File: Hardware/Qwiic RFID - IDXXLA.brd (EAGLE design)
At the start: 25.4 x 34.3 mm, 51 parts, among them J2 SMD, J3 PTH, J4 SMD, J8 AVR_SPI_PROG_3X2TESTPOINTS, Q1 600mA/40V, U1 ATTINY84, U2 ID-12/20SMD

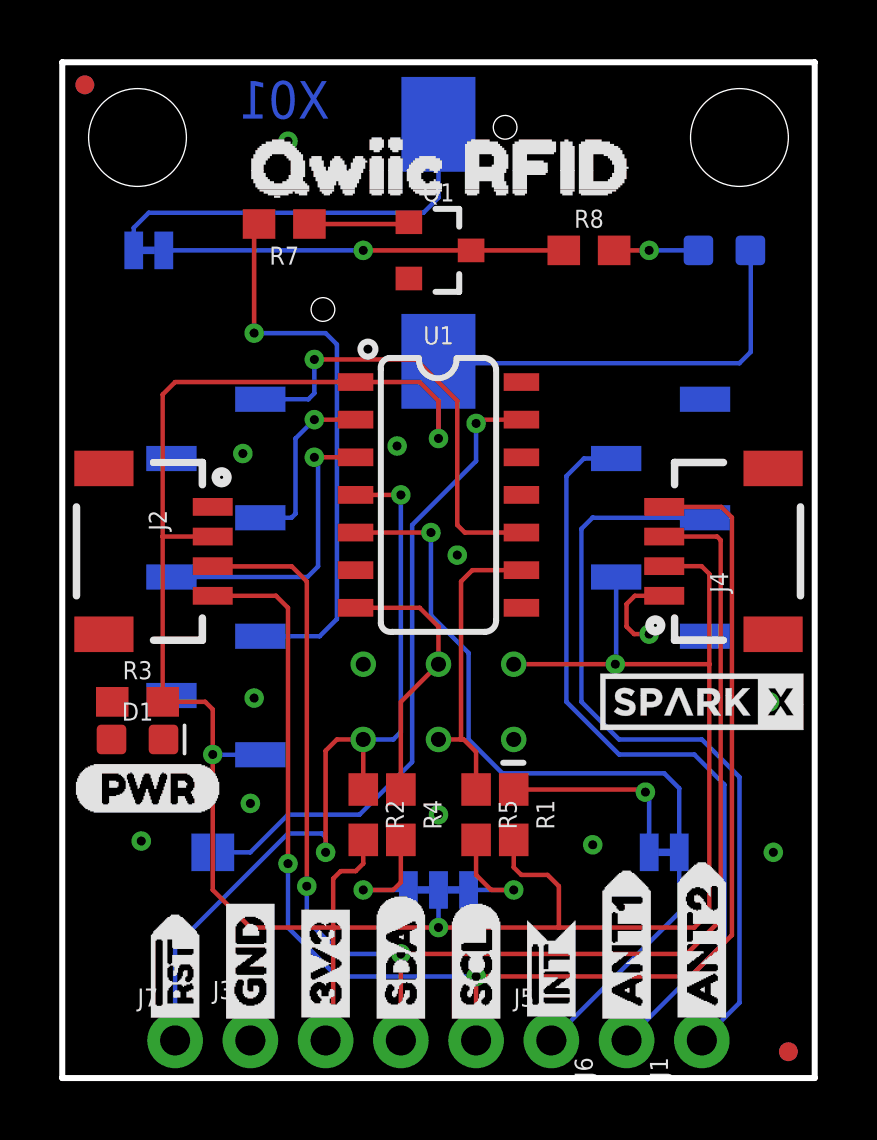
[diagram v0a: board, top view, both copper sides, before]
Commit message: More compact
Shrunk 10 mil, beefed up 3.3V lines to 10 mil
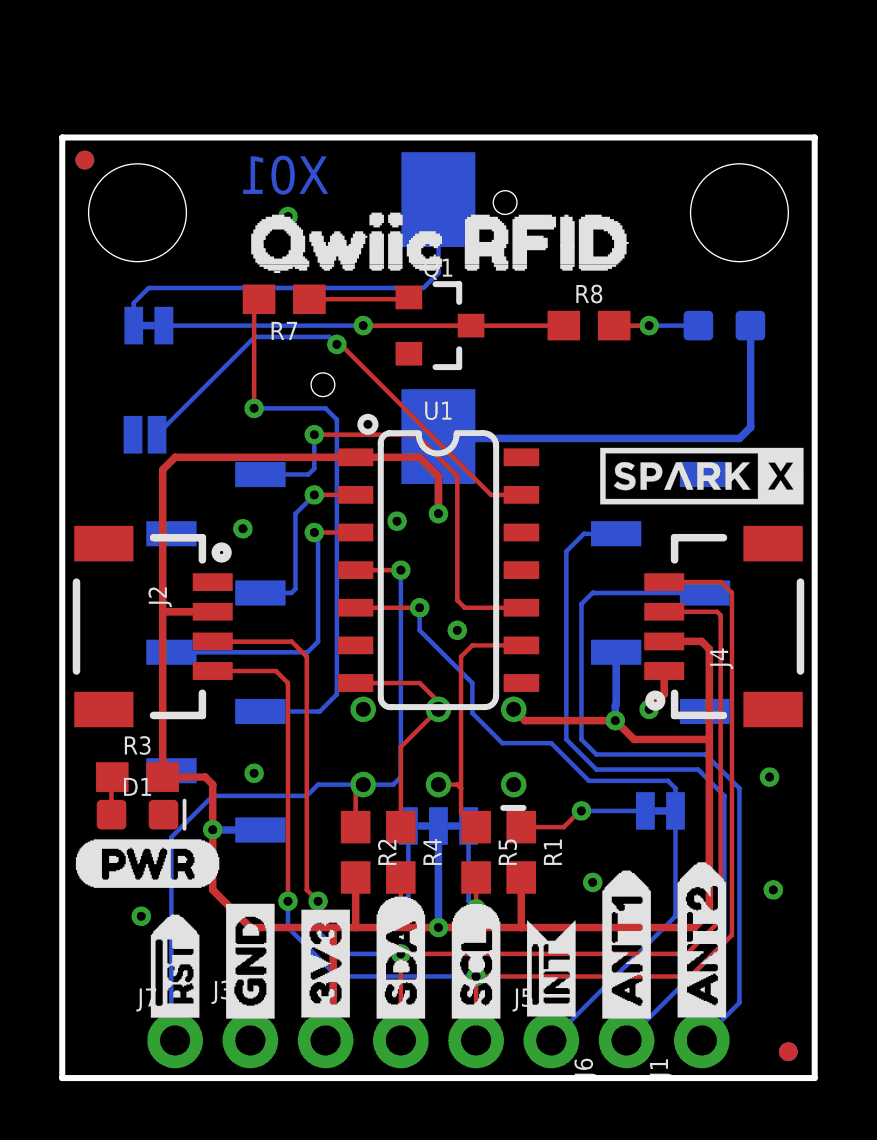
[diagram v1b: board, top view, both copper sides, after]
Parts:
- removed U$14: (no value), Labels:ADR-()
- added U$20: (no value), ANT1:ANT10
- added U$21: (no value), Labels:INT#-[<
- added U$22: (no value), Labels:SCL-[)
- added U$23: (no value), Labels:SDA-[)
- added U$24: (no value), Labels:3V3-04
- added U$25: (no value), Labels:GND-04
- added U$26: (no value), Labels:RST#-[>
- added U$3: (no value), ANT2:ANT20
- U$12: device Labels:I2C-() -> ADR3:ADR0
- U$13: device Labels:INT-() -> INT3:INT0
- U$2: device SparkX:SPARKX-SMALL -> Labels:I_SUPER2_C-()-03
- moved LOGO1 20.3 mm to (18.9, 29.8)
- moved U$12 18.7 mm to (4.70, 19.9)
- moved JP7 14.3 mm to (2.79, 21.7)
- moved U$2 7.73 mm to (14.1, 10.8)
- moved U$4 7.62 mm to (21.6, 20.3)
- moved U$13 5.39 mm to (21.7, 10.9)
- moved D2 2.54 mm to (22.4, 25.4)
- moved JP9 2.54 mm to (2.92, 25.4)
- moved Q1 2.54 mm to (12.7, 25.4)
- moved R8 2.54 mm to (17.8, 25.4)
- moved U$18 2.54 mm to (25.1, 23.7)
- moved U$19 2.54 mm to (4.70, 28.2)
- moved J2 2.54 mm to (5.08, 15.2)
- moved J4 2.54 mm to (20.3, 15.2)
- moved U$1 2.54 mm to (0.38, 7.24)
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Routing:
- net 3.3V: track 102.5 -> 94.9 mm
- net N$6: track 21.5 -> 15.9 mm
- net SDA: track 47.9 -> 42.9 mm
- net SCL: track 49.1 -> 44.0 mm
- net !INT: track 28.2 -> 24.7 mm
- net !RST: track 27.8 -> 25.6 mm, vias 2 -> 1
- net N$4: track 6.57 -> 4.42 mm
- net ANT2: track 26.0 -> 24.0 mm
- net ANT1: track 26.0 -> 24.0 mm
- net GND: track 3.01 -> 1.50 mm, vias 12 -> 10
- net N$3: track 0.00 -> 1.28 mm
- net SDA/MOSI: track 9.09 -> 7.82 mm
- net SCL/SCK: track 10.2 -> 8.97 mm
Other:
- board size 25.4 x 34.3 mm -> 25.4 x 31.8 mm

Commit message: 5 mil smaller
Moved power LED around, squished the PCB a little more.
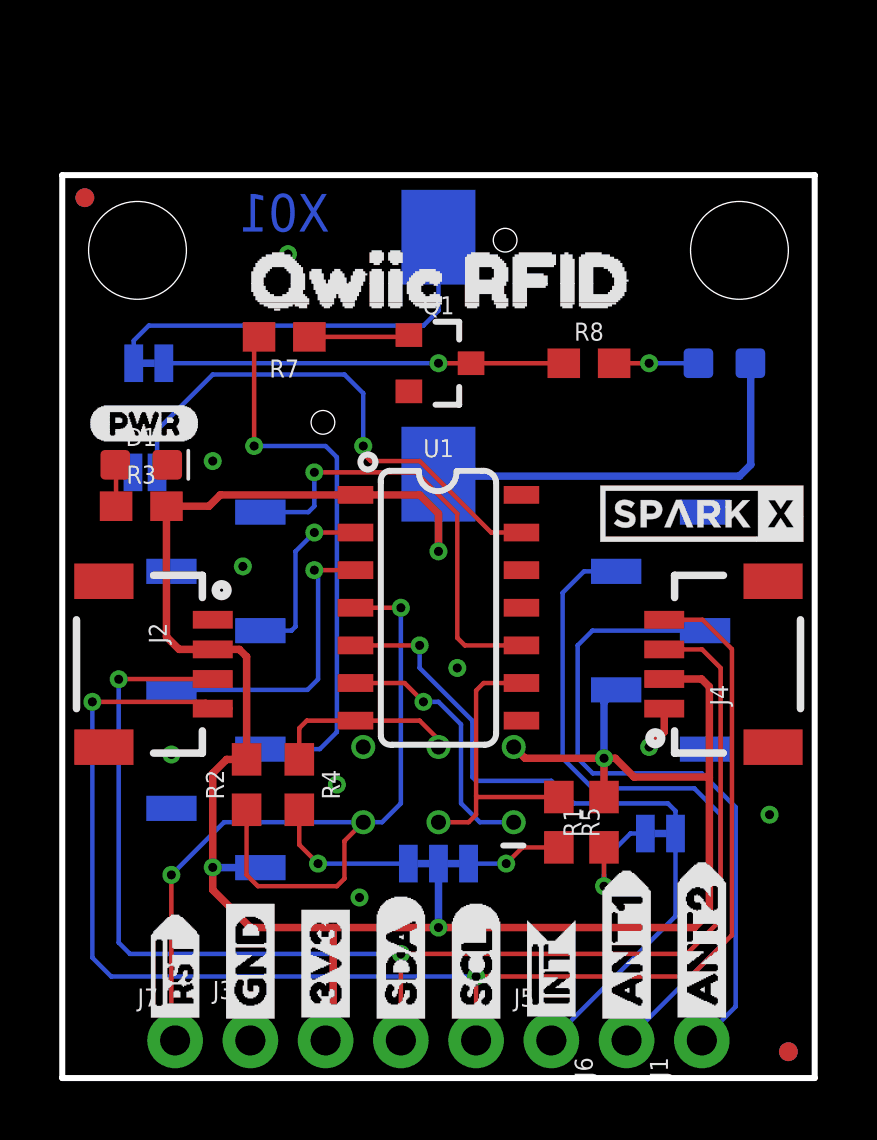
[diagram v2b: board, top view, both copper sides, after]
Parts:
- added U$14: (no value), Labels:PWR-()-03
- U$1: device Labels:PWR-()-04 -> SparkX:SPARKX-TINY
- moved U$1 23.1 mm to (7.62, 29.2), flipped to the bottom
- moved D1 11.8 mm to (2.67, 20.7)
- moved R3 9.14 mm to (2.67, 19.3)
- moved U$13 5.50 mm to (18.2, 6.73), turned to 90 degrees
- moved R2 4.33 mm to (6.22, 9.91), turned to 90 degrees
- moved R4 4.12 mm to (8.00, 9.91)
- moved R1 2.97 mm to (18.3, 8.64), turned to 90 degrees
- moved R5 2.97 mm to (16.8, 8.64)
- moved U$12 1.33 mm to (4.32, 18.7)
- moved R7 1.27 mm to (7.49, 25.0)
- moved U2 1.27 mm to (12.7, 14.1)
- moved I2C 1.27 mm to (12.7, 7.24)
- moved D2 1.27 mm to (22.4, 24.1)
- moved J2 1.27 mm to (5.08, 14.0)
- moved J4 1.27 mm to (20.3, 14.0)
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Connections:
- net MISO: now also U1.6
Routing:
- net MISO: track 0.00 -> 8.85 mm, vias 0 -> 1
- net SCL: track 44.0 -> 50.3 mm
- net 3.3V: track 94.9 -> 89.0 mm
- net !RST: track 25.6 -> 31.1 mm, vias 1 -> 2
- net SDA: track 42.9 -> 47.1 mm
- net N$6: track 15.9 -> 17.9 mm
- net SDA/MOSI: track 7.82 -> 6.38 mm
- net ANT1: track 24.0 -> 22.7 mm
- net ANT2: track 24.0 -> 22.8 mm
- net N$2: track 3.95 -> 5.13 mm
- net SCL/SCK: track 8.97 -> 10.0 mm
- net N$1: track 3.95 -> 3.27 mm
- net GND: vias 10 -> 9
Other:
- board size 25.4 x 31.8 mm -> 25.4 x 30.5 mm

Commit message: Moved RST clost to INT PTH, better routing
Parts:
- added C1: 0.1uF, SparkFun-Capacitors:0603
- U1: value ATTINY84 -> ATTINY84-ARDUINO
- moved J7 10.2 mm to (14.0, 1.27)
- moved U$26 10.2 mm to (14.0, 1.40)
- moved U$5 10.2 mm to (14.0, 1.40)
- moved U$10 2.54 mm to (6.35, 1.52)
- moved U$22 2.54 mm to (11.4, 1.52)
- moved U$24 2.54 mm to (6.35, 1.52)
- moved U$7 2.54 mm to (11.4, 1.52)
- moved J3 2.54 mm to (3.81, 1.27)
- moved U$25 2.54 mm to (3.81, 1.52)
- moved U$9 2.54 mm to (3.81, 1.52)
- moved U$23 2.54 mm to (8.89, 1.52)
- moved U$6 2.54 mm to (8.89, 1.52)
- moved R2 0.76 mm to (6.99, 9.91)
- moved R4 0.63 mm to (8.64, 9.91)
- moved R1 0.51 mm to (18.3, 9.14)
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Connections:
- net DO renamed DATA_UART
- removed net D1: U1.2, U2.8
- net !INT: now also U1.10; no longer U1.5
- net 3.3V: now also C1.1
- net GND: now also C1.2
- net MISO: now also U1.8; no longer U1.6
- net TAG_IN_RANGE: now also U1.5; no longer U1.10
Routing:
- net SCL: track 50.3 -> 42.2 mm, vias 2 -> 1
- net TAG_IN_RANGE: track 14.9 -> 7.67 mm
- net D1: track 6.07 -> 0.00 mm, vias 1 -> 0
- net SDA: track 47.1 -> 42.4 mm, vias 2 -> 1
- net !RST: track 31.1 -> 27.8 mm
- net !INT: track 24.3 -> 21.8 mm
- net MISO: track 8.85 -> 6.79 mm
- net ANT1: track 22.7 -> 20.9 mm
- net ANT2: track 22.8 -> 21.2 mm
- net LED_BUZZ: track 18.8 -> 17.4 mm
- net 3.3V: track 89.0 -> 88.3 mm, vias 4 -> 5
- net SDA/MOSI: track 6.38 -> 5.67 mm
- net N$1: track 3.27 -> 3.95 mm
- net N$4: track 4.34 -> 4.85 mm
- net GND: vias 9 -> 17
